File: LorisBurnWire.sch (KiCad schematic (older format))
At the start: 25 parts, among them SW1 SW_SPST, U1 ADP2303, U2 TLC555, U3 TLC555

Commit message: init_commit
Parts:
- removed C6, C8, C?: 0.01uF, symbol Device:CP1
- removed C7, C8: 10 uF, symbol Device:CP1
- added C? (x3): 0.01uF, symbol Device:C
- added C? (x2): 10uF, symbol Device:C
- added R?: Heater, symbol Device:Heater
- U1: symbol Loris:ADP2303 -> LorisBurnWire-rescue:ADP2303-Loris
- U2, U3: symbol Loris:TLC555 -> LorisBurnWire-rescue:TLC555-Loris
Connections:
- net labels added: GNDA, GNDD
- net labels removed: GND, GNDREF
- wire segments 115 -> 105
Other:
- moved on the sheet: C1, C2, C3, C4, C5, D1, D2, L1, R1, R2, R3

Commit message: changes
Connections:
- wire segments 105 -> 104
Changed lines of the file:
@@
 $EndComp
-Wire Wire Line
-	6225 2300 6225 2450
-Wire Wire Line
-	7025 2300 7025 2450
 Wire Wire Line
 	6225 2000 6625 2000
@@
 Wire Wire Line
 	5825 2000 6225 2000
-Wire Wire Line
-	6625 2300 6625 2450
-Connection ~ 6625 2450
-Wire Wire Line
-	6625 2450 6225 2450
-Wire Wire Line
-	6625 2450 7025 2450
-Wire Wire Line
-	6625 2800 6625 2450
 Connection ~ 4550 2800
 $Comp
@@
 $EndComp
 Wire Wire Line
-	6625 2800 7800 2800
-Wire Wire Line
 	7800 2800 7800 2575
-Connection ~ 6625 2800
 Wire Wire Line
 	7800 2275 7800 2000
@@
 Connection ~ 5125 2800
 Wire Wire Line
-	5125 2800 6625 2800
+	5125 2800 6225 2800
+Wire Wire Line
+	6225 2300 6225 2800
+Connection ~ 6225 2800
+Wire Wire Line
+	6225 2800 6625 2800
+Wire Wire Line
+	6625 2300 6625 2800
+Connection ~ 6625 2800
+Wire Wire Line
+	6625 2800 7025 2800
+Wire Wire Line
+	7025 2300 7025 2800
+Connection ~ 7025 2800
+Wire Wire Line
+	7025 2800 7800 2800
 $EndSCHEMATC

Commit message: added_bjt
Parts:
- removed SW1: SW_SPST, symbol Switch:SW_SPST
- added C10, C20, C21, C22, C23, C24, C25, C8, C9: 47uF, symbol Device:CP1
- added C15, C16, C6: 10uF, symbol Device:C
- added C18, C19, C7: 0.1uF, symbol Device:C
- added D4, D5, D6, D7, D8, D9: D, symbol Device:D
- added L2, L3, L4: 6uH, symbol pspice:INDUCTOR
- added Q1: 2SC370700L, symbol LorisBurnWire-rescue:2SC370700L
- added R10, R17, R18: 0.5, symbol Device:R_US
- added R11, R19, R20: Heater, symbol Device:Heater
- added R13, R14, R15, R16, R8, R9: 10K, symbol Device:R_US
- added U4, U5, U6: ADP2303, symbol LorisBurnWire-rescue:ADP2303-Loris
- gave numbers to parts that had none: 6
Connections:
- net labels added: 30_MIN_TIMER
- net labels removed: ENABLE?
- wire segments 104 -> 235
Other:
- note added: "Panel 1 and Panel 2"
- note added: "Panel 3 and Panel 4"
- moved on the sheet: C1, C11, C12, C13, C14, C17, C2, C3, C4, C5, D1, D2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

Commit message: practice
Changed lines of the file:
@@
 	800  625  800  8775
 Connection ~ 8325 1650
+Text Label 10100 1400 0    50   ~ 0
+Test
 $EndSCHEMATC

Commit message: fixxed_error
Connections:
- net WireCutter1: no longer C12.1, R5.2, U2.6 (THRES), U2.7 (DISCH)
- new net: C12.1, R5.2, U2.6 (THRES), U2.7 (DISCH)
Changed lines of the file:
@@
 Wire Wire Line
 	8175 1850 8175 2050
-Connection ~ 8175 1850
 Wire Wire Line
 	8175 2300 8175 2050
 Connection ~ 8175 2050
-Wire Wire Line
-	8175 1200 8175 1650
 Wire Wire Line
 	7675 2650 8175 2650
@@
 Text GLabel 5675 1975 1    50   Input ~ 0
 30_MIN_TIMER
-Connection ~ 8175 1650
-Wire Wire Line
-	8175 1650 8175 1850
 Wire Wire Line
 	10075 1650 10075 3000
@@
 Text Label 10100 1400 0    50   ~ 0
 Test
+Wire Wire Line
+	8175 1850 8250 1850
+Wire Wire Line
+	8250 1850 8250 1500
+Wire Wire Line
+	8250 1500 8175 1500
+Wire Wire Line
+	8175 1500 8175 1200
+Connection ~ 8175 1850
 $EndSCHEMATC

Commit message: moddy
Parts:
- removed D1, D4, D5, D6, D7, D8, D9: D, symbol Device:D
- removed R11, R19, R20: Heater, symbol Device:Heater
- added D? (x3): B330B-13-F, symbol Device:D
- added R? (x3): Nichrome wire, symbol Device:Heater
- D2: value D -> B330B-13-F
- R12: value Heater -> Nichrome wire
- R4: value 33K -> 2M
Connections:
- net GNDA: now also D?.2 (A), D?.2 (A), D?.2 (A), R?.2, R?.2, R?.2
- net PACK+: now reaches C1.1, R1.2, U1.2 (Vin)
- net PACK+: now also C15.1, C16.1, C6.1, R13.2, R14.2, R8.2, U4.2 (Vin), U5.2 (Vin), U6.2 (Vin)
- net +5V: now reaches D3.1 (K), R4.1, R5.1, R6.1, R7.1, U2.4 (RESET), U2.8 (VDD), U3.4 (RESET), U3.8 (VDD)
- net at C19.2, L4.1, U6.8 (SW): now also D?.1 (K)
- net at C21.1, C23.1, C25.1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: now also R?.1
- net at C7.2, L2.1, U4.8 (SW): now also D?.1 (K)
- net at C10.1, C8.1, C9.1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: now also R?.1
- net at C18.2, L3.1, U5.8 (SW): now also D?.1 (K)
- net at C20.1, C22.1, C24.1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: now also R?.1
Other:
- moved on the sheet: C15, C16, C18, C19, C20, C21, C22, C23, C24, C25, L3, L4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

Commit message: started_pcb
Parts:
- removed C10, C20, C21, C22, C23, C24, C25, C3, C4, C5, C8, C9: 47uF, symbol Device:CP1
- removed D? (x3): B330B-13-F, symbol Device:D
- removed R12, R? (x3): Nichrome wire, symbol Device:Heater
- removed R17, R18: 0.5, symbol Device:R_US
- removed R4: 2M, symbol Device:R_US
- added C10, C20, C21, C22, C23, C24, C25, C5, C8, C9: 47uF, Capacitor_SMD:C_1206_3216Metric_Pad1.42x1.75mm_HandSolder, symbol Device:C
- added C3: 10uF, Capacitor_SMD:C_1206_3216Metric_Pad1.42x1.75mm_HandSolder, symbol Device:C
- added C4: 0.1uF, Capacitor_SMD:C_1206_3216Metric_Pad1.42x1.75mm_HandSolder, symbol Device:C
- added D1, D4, D5: B330B-13-F, Diode_SMD:D_SMB_Handsoldering, symbol Device:D
- added J1, J2, J3, J4: Screw_Terminal_01x02, TerminalBlock_Phoenix:TerminalBlock_Phoenix_MKDS-3-2-5.08_1x02_P5.08mm_Horizontal, symbol Connector:Screw_Terminal_01x02
- added J5: Conn_01x02_Male, Connector_PinSocket_2.54mm:PinSocket_1x02_P2.54mm_Vertical, symbol Connector:Conn_01x02_Male
- added R11, R12: 10K, Resistor_SMD:R_1206_3216Metric_Pad1.42x1.75mm_HandSolder, symbol Device:R_US
- C1, C11, C12, C13, C14, C15, C16, C17, C18, C19, C2: footprint (none) -> Capacitor_SMD:C_1206_3216Metric_Pad1.42x1.75mm_HandSolder
- C6: value 10uF -> 47uF; footprint (none) -> Capacitor_SMD:C_1206_3216Metric_Pad1.42x1.75mm_HandSolder
- C7: value 0.1uF -> 47uF; footprint (none) -> Capacitor_SMD:C_1206_3216Metric_Pad1.42x1.75mm_HandSolder
- D2: footprint (none) -> Diode_SMD:D_SMB_Handsoldering
- D3: value D -> 1N4148W-13-F; footprint (none) -> Diodes_SMD:D_SOD-123
- L1, L2, L3, L4: value 6uH -> 5.2uH; footprint (none) -> TempoFootprints:CDRH104RNP-5R2NC; Part Number (none) -> CDRH104RNP-5R2NC
- Q1: footprint (none) -> Package_TO_SOT_SMD:SC-59_Handsoldering
- R1, R10, R13, R14, R2, R3, R5, R6, R7, R8, R9: footprint (none) -> Resistor_SMD:R_1206_3216Metric_Pad1.42x1.75mm_HandSolder
- R15, R16: value 10K -> 0.5; footprint (none) -> Resistor_SMD:R_1206_3216Metric_Pad1.42x1.75mm_HandSolder
- U1, U4, U5, U6: footprint (none) -> Package_SO:SOIC-8-1EP_3.9x4.9mm_P1.27mm_EP2.29x3mm
- U2, U3: value TLC555 -> TLC555ID; footprint (none) -> Housings_SOIC:SOIC-8_3.9x4.9mm_Pitch1.27mm
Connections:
- net +5V: now also J5.1 (Pin_1)
- net GNDA: now also C7.2, R15.1, R16.1, C10.2, C20.2, C21.2, C22.2, C23.2, C24.2, C25.2, C3.2, C5.2, C8.2, C9.2, D1.2 (A), D4.2 (A), D5.2 (A), J1.2 (Pin_2), J2.2 (Pin_2), J3.2 (Pin_2), J4.2 (Pin_2)
- net PACK+: now also C3.1, R11.2, R12.2; no longer C6.1, R13.2, R14.2
- net WireCutter1: now also U5.3 (EN); no longer U6.3 (EN)
- net WireCutter2: now also U6.3 (EN); no longer U5.3 (EN)
- net at L1.2: now also C7.1, C10.1, C9.1, J2.1 (Pin_1)
- net at Q1.3 (C), U2.2 (TRIG): now also J5.2 (Pin_2)
- net at C19.2, L4.1, U6.8 (SW): now also D5.1 (K)
- net at C18.2, L3.1, U5.8 (SW): now also D4.1 (K)
- net at U6.4 (PGood): now also R12.1; no longer R14.1
- net at U6.5 (FB): now also R14.2; no longer R16.2
- net at L4.2: now also C21.1, C23.1, C25.1, J4.1 (Pin_1)
- net at L2.1, U4.8 (SW): now also C4.2, D1.1 (K); no longer C7.2
- net at L3.2: now also C20.1, C22.1, C24.1, J3.1 (Pin_1)
- net at L2.2: now also C6.1, C5.1, C8.1, J1.1 (Pin_1)
- net at U4.1 (BST): now also C4.1; no longer C7.1
- net at U5.4 (PGood): now also R11.1; no longer R13.1
- net at U5.5 (FB): now also R13.2; no longer R15.2
- new net: R13.1, R15.2
- new net: R14.1, R16.2
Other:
- moved on the sheet: C1, C2, D2, L1, R1, R2, R3, U1

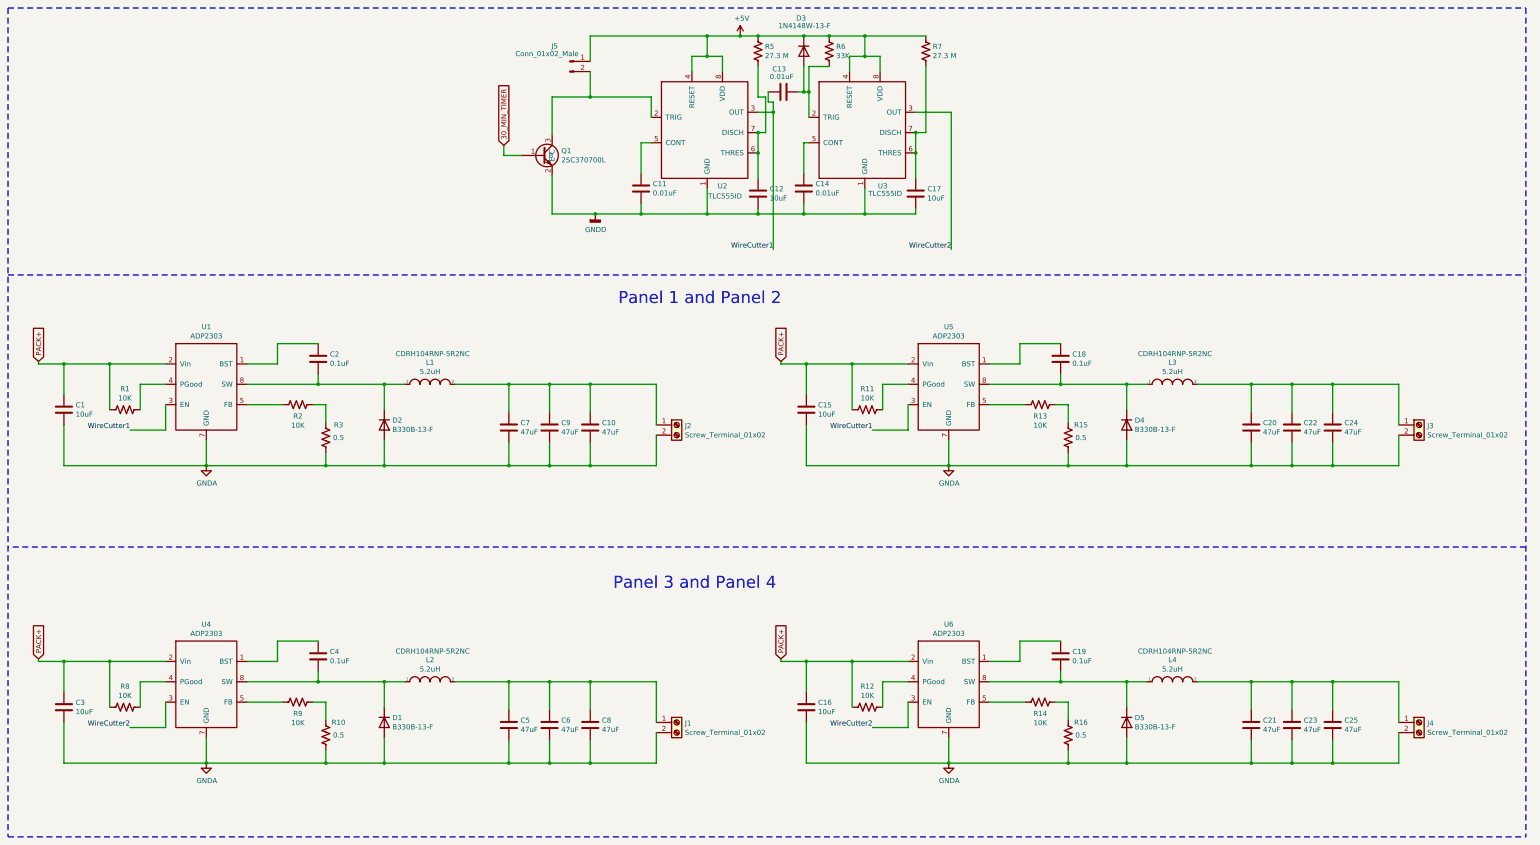
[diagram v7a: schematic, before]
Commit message: added precicion current limiter
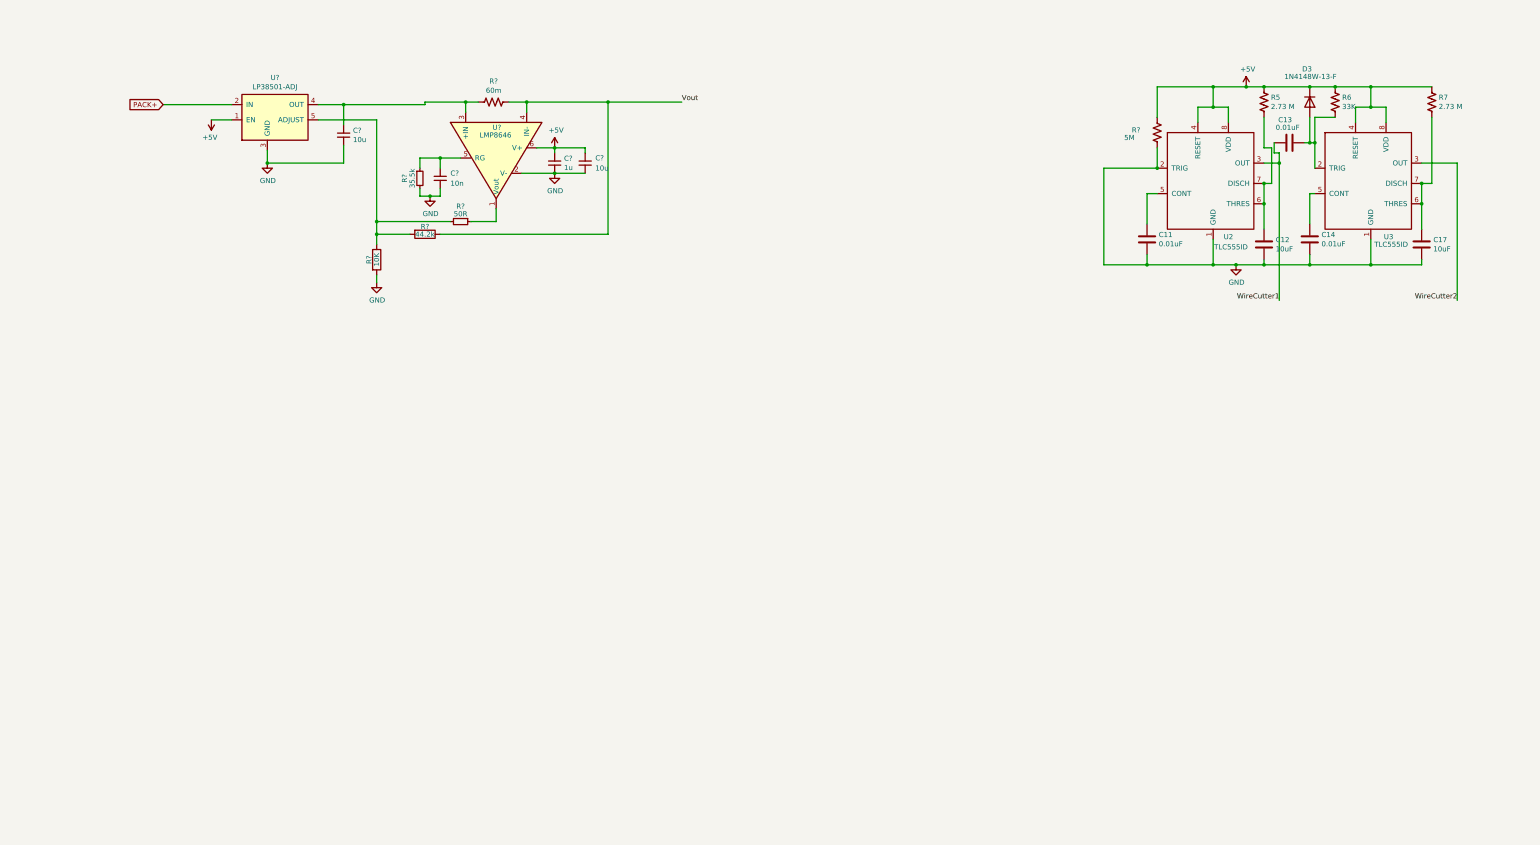
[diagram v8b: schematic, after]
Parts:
- removed C1, C15, C16, C3: 10uF, Capacitor_SMD:C_1206_3216Metric_Pad1.42x1.75mm_HandSolder, symbol Device:C
- removed C10, C20, C21, C22, C23, C24, C25, C5, C6, C7, C8, C9: 47uF, Capacitor_SMD:C_1206_3216Metric_Pad1.42x1.75mm_HandSolder, symbol Device:C
- removed C18, C19, C2, C4: 0.1uF, Capacitor_SMD:C_1206_3216Metric_Pad1.42x1.75mm_HandSolder, symbol Device:C
- removed D1, D2, D4, D5: B330B-13-F, Diode_SMD:D_SMB_Handsoldering, symbol Device:D
- removed J1, J2, J3, J4: Screw_Terminal_01x02, TerminalBlock_Phoenix:TerminalBlock_Phoenix_MKDS-3-2-5.08_1x02_P5.08mm_Horizontal, symbol Connector:Screw_Terminal_01x02
- removed J5: Conn_01x02_Male, Connector_PinSocket_2.54mm:PinSocket_1x02_P2.54mm_Vertical, symbol Connector:Conn_01x02_Male
- removed L1, L2, L3, L4: 5.2uH, TempoFootprints:CDRH104RNP-5R2NC, symbol pspice:INDUCTOR
- removed Q1: 2SC370700L, Package_TO_SOT_SMD:SC-59_Handsoldering, symbol LorisBurnWire-rescue:2SC370700L
- removed R1, R11, R12, R13, R14, R2, R8, R9: 10K, Resistor_SMD:R_1206_3216Metric_Pad1.42x1.75mm_HandSolder, symbol Device:R_US
- removed R10, R15, R16, R3: 0.5, Resistor_SMD:R_1206_3216Metric_Pad1.42x1.75mm_HandSolder, symbol Device:R_US
- removed U1, U4, U5, U6: ADP2303, Package_SO:SOIC-8-1EP_3.9x4.9mm_P1.27mm_EP2.29x3mm, symbol LorisBurnWire-rescue:ADP2303-Loris
- added C? (x2): 10u, symbol Device:C_Small
- added C?: 1u, symbol Device:C_Small
- added C?: 10n, symbol Device:C_Small
- added R?: 5M, Resistor_SMD:R_1206_3216Metric_Pad1.42x1.75mm_HandSolder, symbol Device:R_US
- added R?: 60m, symbol Device:R_US
- added R?: 50R, symbol Device:R_Small
- added R?: 10K, symbol Device:R
- added R?: 44.2k, symbol Device:R
- added R?: 35.5k, symbol Device:R_Small
- added U?: LMP8646, symbol BurnWireLib:LMP8646
- added U?: LP38501-ADJ, symbol BurnWireLib:LP38501-ADJ
- R5, R7: value 27.3 M -> 2.73 M
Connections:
- net GNDD is gone; now on net GND: C11.2, C12.2, C14.2, C17.2, U2.1 (GND), U3.1 (GND)
- net +5V: now also C?.1, C?.2, R?.1, U?.1 (EN), U?.6 (V+)
- net PACK+: now also U?.2 (IN)
- net GND: now reaches U2.2 (TRIG)
- net GND: now also C?.1, C?.1, C?.2, C?.2, R?.2, R?.2, R?.2, U?.2 (V-), U?.3 (GND)
- new net: R?.1, U?.1 (Vout)
- new net: C?.2, R?.2, U?.3 (+IN), U?.4 (OUT)
- new net: C?.1, R?.1, U?.5 (RG)
- new net: R?.1, R?.2, R?.2, U?.5 (ADJUST)
- new net Vout: R?.1, R?.1, U?.4 (IN-)
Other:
- note removed: "Panel 1 and Panel 2"
- note removed: "Panel 3 and Panel 4"
- moved on the sheet: C11, C12, C13, C14, C17, D3, R5, R6, R7, U2, U3
